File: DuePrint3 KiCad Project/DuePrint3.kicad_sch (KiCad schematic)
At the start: 49 parts, among them J1 MF3.0-2x12-430452412, J10 MF3.0-1x2-436500215, J11 2.54Header-1x2-M, J12 2.54Header-1x2-M, J13 EHT-125-01-S-D, J14 EHT-110-01-S-D, J15 EHT-125-01-S-D, J2 2.54Header-1x16-F, J3 2.54Header-1x16-F, J4 6P2C, J5 6P2C, J6 2.54Header-1x3-M, J7 MF3.0-1x2-436500215, J8 MF3.0-1x8-436500815, J9 MF3.0-2x9-430451812, U1 SN74AHCT125DR

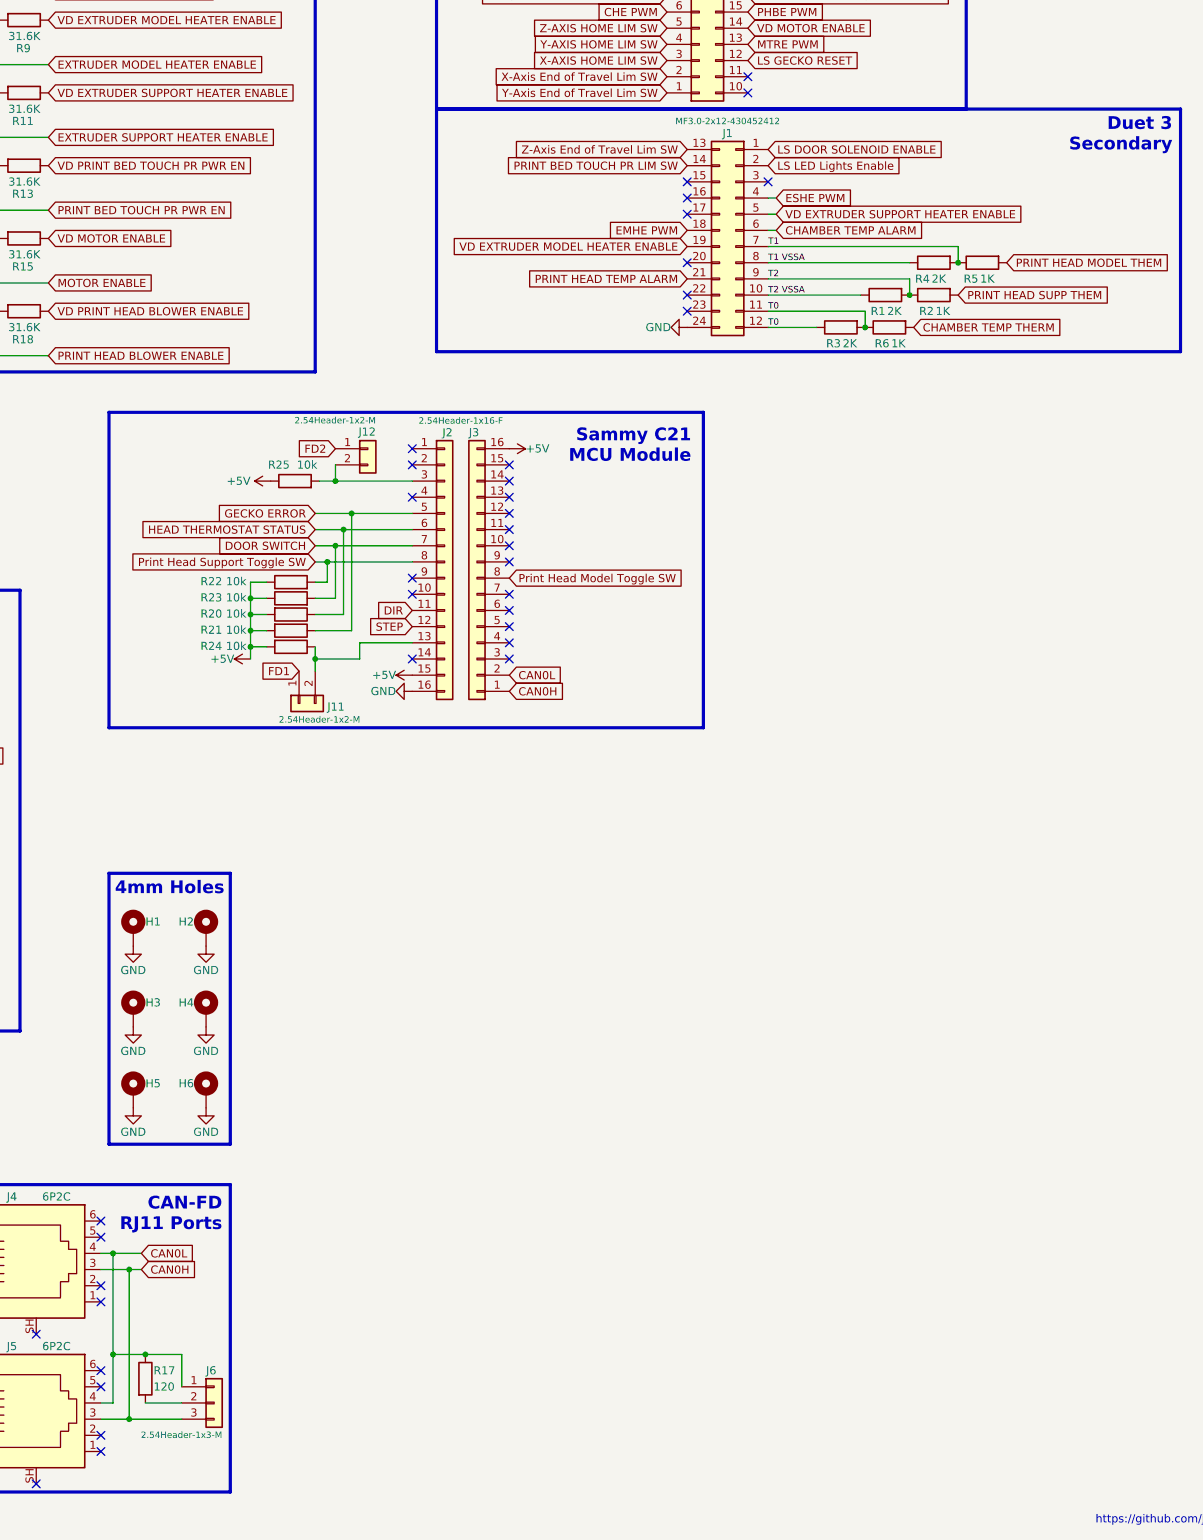
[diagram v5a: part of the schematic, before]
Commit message: Footprint & Symbol reorg; PCB & Schematic now cleaned-up
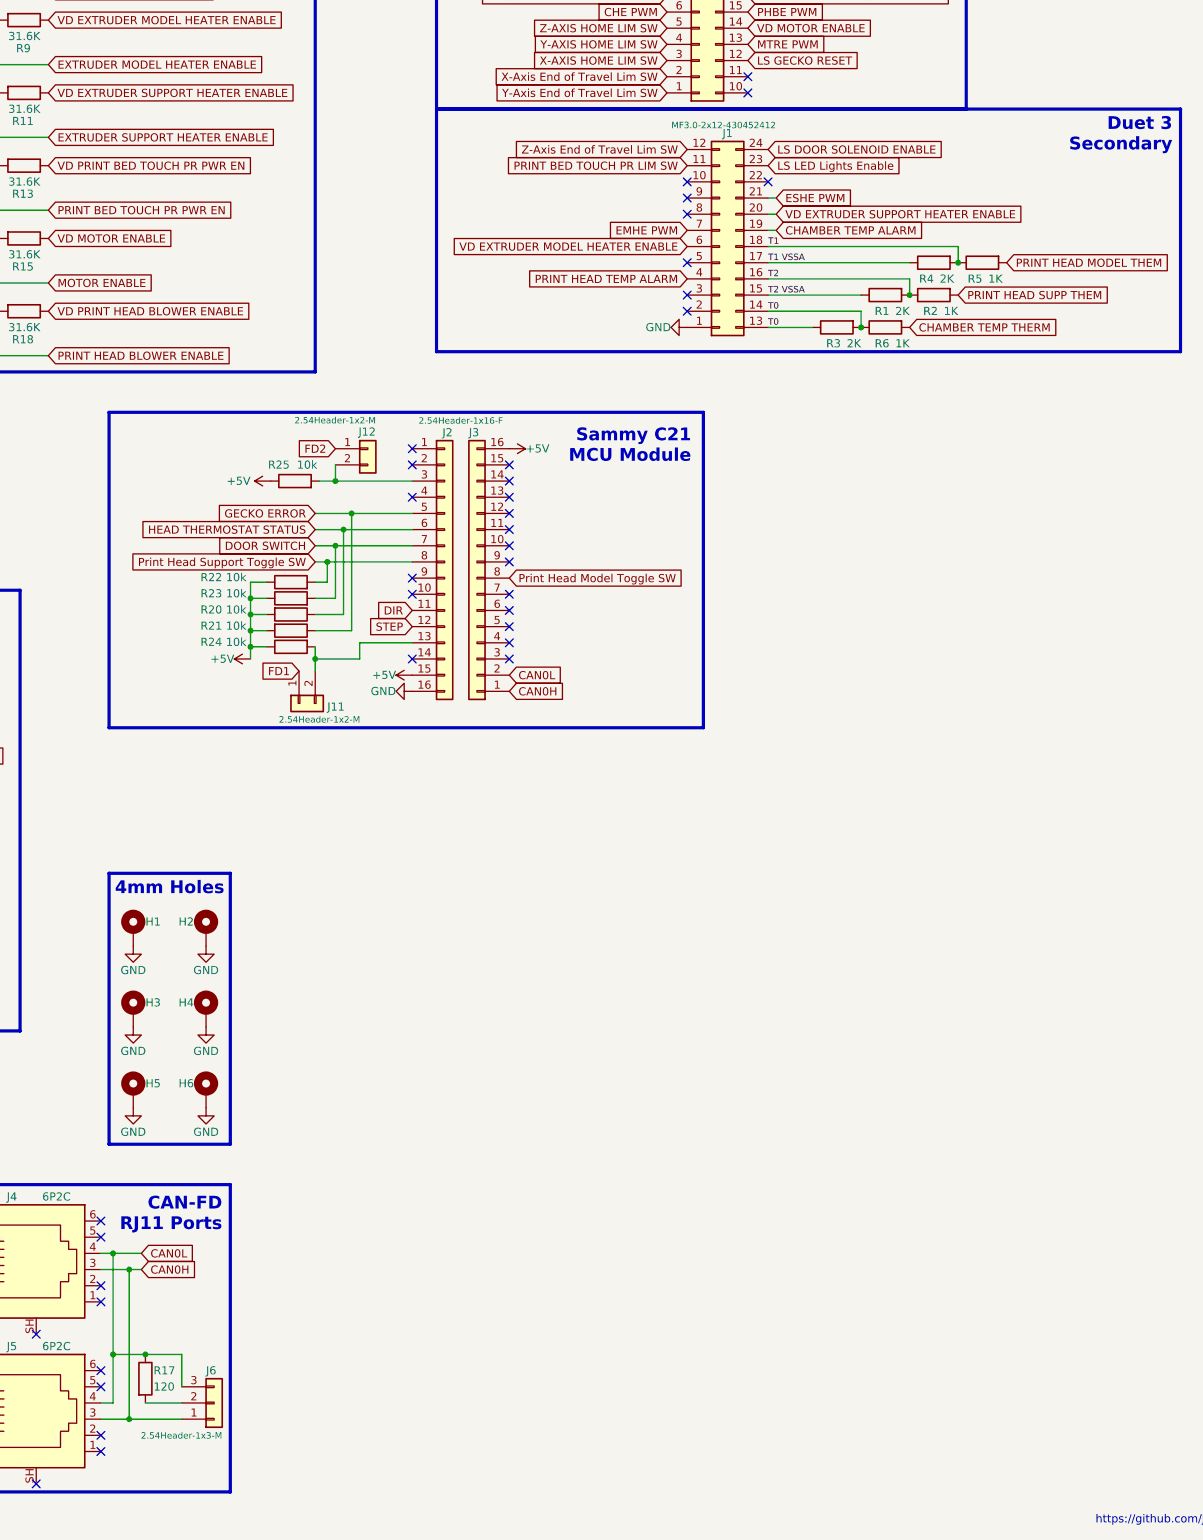
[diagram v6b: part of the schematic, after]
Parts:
- J13, J15: footprint EHT-125-01-S-D:SAMTEC_EHT-125-01-S-D -> DuePrint3-Lib:SAMTEC_EHT-125-01-S-D
- J14: footprint EHT-110-01-XX-D:EHT-110-01-XX-D -> DuePrint3-Lib:EHT-110-01-XX-D
- J2, J3: footprint (none) -> Connector_PinSocket_2.54mm:PinSocket_1x16_P2.54mm_Vertical
- J6: footprint (none) -> Connector_PinHeader_2.54mm:PinHeader_1x03_P2.54mm_Vertical
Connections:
- net +5V: now also R24.1; no longer R24.2
- net CAN0H: now also J6.1 (Pin_1); no longer J6.3 (Pin_3)
- net CAN0L: now also J6.3 (Pin_3); no longer J6.1 (Pin_1)
- net CHAMBER TEMP ALARM: now also J1.19 (Pin_19); no longer J1.6 (Pin_6)
- net EMHE PWM: now also J1.7 (Pin_7); no longer J1.18 (Pin_18)
- net ESHE PWM: now also J1.21 (Pin_21); no longer J1.4 (Pin_4)
- net GND: now also J1.1 (Pin_1); no longer J1.24 (Pin_24)
- net LS DOOR SOLENOID ENABLE: now also J1.24 (Pin_24); no longer J1.1 (Pin_1)
- net LS LED Lights Enable: now also J1.23 (Pin_23); no longer J1.2 (Pin_2)
- net PRINT BED TOUCH PR LIM SW: now also J1.11 (Pin_11); no longer J1.14 (Pin_14)
- net PRINT HEAD TEMP ALARM: now also J1.4 (Pin_4); no longer J1.21 (Pin_21)
- net T0: now also J1.13 (Pin_13), J1.14 (Pin_14); no longer J1.11 (Pin_11), J1.12 (Pin_12)
- net T1: now also J1.18 (Pin_18); no longer J1.7 (Pin_7)
- net T1 VSSA: now also J1.17 (Pin_17); no longer J1.8 (Pin_8)
- net T2: now also J1.16 (Pin_16); no longer J1.9 (Pin_9)
- net T2 VSSA: now also J1.15 (Pin_15); no longer J1.10 (Pin_10)
- net VD EXTRUDER MODEL HEATER ENABLE: now also J1.6 (Pin_6); no longer J1.19 (Pin_19)
- net VD EXTRUDER SUPPORT HEATER ENABLE: now also J1.20 (Pin_20); no longer J1.5 (Pin_5)
- net Z-Axis End of Travel Lim SW: now also J1.12 (Pin_12); no longer J1.13 (Pin_13)
- net at J11.2 (Pin_2), J2.13 (Pin_13): now also R24.2; no longer R24.1
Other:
- moved on the sheet: R24, R3, R6
